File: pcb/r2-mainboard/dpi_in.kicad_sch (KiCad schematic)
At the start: 0 parts

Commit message: R2: WP7 -- dpi_in drawn, and a silent short caught before it reached fab
tools/gen_dpi_in.py draws dpi_in.kicad_sch: unit 2 of the PCM-071, 22 pins
fanning into the 22 hierarchical labels fpga_io has exported since WP5. No
components at all, which is also how the "nothing may load DPI_R6/DPI_R7" rule
is satisfied -- a sheet note says so, so a later reviewer does not add the
"missing" termination.

The bit mapping is the whole content of the sheet and the only thing that can
be wrong in a way that still boots: VOUT0_DATA<n> = DPI_PIXEL[n], channel =
BGR[n/6], bit = 2 + n%6, where the 2 is RGB666 keeping the top six bits of each
channel. Verified three ways -- the generator asserts the 22 net names are
exactly the expected set with no duplicates and that D2/D4 land on R6/R7; every
claimed pin is re-read from som_pinout.json; and the exported netlist is
cross-checked against Caster's own UCF, where all 18 DPI_PIXEL LOC constraints
land on the ball the schematic wires.

A REAL BUG, found by that netlist check and not by ERC. set_sheet_pins grew
dpi_in's root box from 25.4 mm to 63.5 mm to fit 22 pins, and the taller box
swallowed epd's. wire_root's stubs then landed inside epd's box and merged the
two sheets' nets: seven DPI_* nets came out shorted to the panel bus, so
DPI_R2 was the same net as EPDC_D0N, with J6.38 and a second U41 ball on it.
The schematic stayed perfectly legal and ERC said nothing.

This is the *second* time -- WP5 lost seven FPGA balls to VCOM_MEA_EN the same
way when fpga_io grew. The guard existed but lived in layout_root.py, which
nothing was obliged to call. Moved: layout_root.overlaps()/assert_no_overlap()
are now the shared implementation, and wire_root.py calls it before emitting
anything. wire_root is the right home because it is what turns sheet pins into
nets, so it is the last place the check can prevent the short rather than
report it afterwards. Confirmed the guard fires on the broken tree, then
layout_root re-packed the column and eve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
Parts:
- added X2: PCM-071, footprints:PCM-071_2xBTH-060-01-L-D-A-K, symbol r2:PCM-071
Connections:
- new net DPI_B2: X2.B12 (X_VOUT0_DATA0)
- new net DPI_B3: X2.B6 (X_VOUT0_DATA1)
- new net DPI_B4: X2.B4 (X_VOUT0_DATA2)
- new net DPI_B5: X2.B5 (X_VOUT0_DATA3)
- new net DPI_B6: X2.B7 (X_VOUT0_DATA4)
- new net DPI_B7: X2.B10 (X_VOUT0_DATA5)
- new net DPI_DE: X2.A15 (X_VOUT0_DE)
- new net DPI_G2: X2.B11 (X_VOUT0_DATA6)
- new net DPI_G3: X2.B9 (X_VOUT0_DATA7)
- new net DPI_G4: X2.B15 (X_VOUT0_DATA8)
- new net DPI_G5: X2.B14 (X_VOUT0_DATA9)
- new net DPI_G6: X2.A16 (X_VOUT0_DATA10)
- new net DPI_G7: X2.A11 (X_VOUT0_DATA11)
- new net DPI_HS: X2.A6 (X_VOUT0_HSYNC)
- new net DPI_PCLK: X2.A7 (X_VOUT0_PCLK)
- new net DPI_R2: X2.A8 (X_VOUT0_DATA12)
- new net DPI_R3: X2.A10 (X_VOUT0_DATA13)
- new net DPI_R4: X2.A12 (X_VOUT0_DATA14)
- new net DPI_R5: X2.A13 (X_VOUT0_DATA15)
- new net DPI_R6: X2.D2 (X_GPMC0_AD8/BOOTMODE_8)
- new net DPI_R7: X2.D4 (X_GPMC0_AD9/BOOTMODE_9)
- new net DPI_VS: X2.A5 (X_VOUT0_VSYNC)
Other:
- note added: "*** D2 and D4 are also BOOTMODE_8 and BOOTMODE_9, the primary boot mode"
- note added: "*** The absence of components here is deliberate. See docs/som.md 2."
- note added: "*** may load DPI_R6 or DPI_R7 -- no pull-up, pull-down or termination."
- note added: "*** selection, strapped high by 100K on the module. Nothing on this board"
- note added: "Bit mapping, from AM62x TRM Fig. 12-471 and Caster constraint.ucf:"
- note added: "RGB666 keeps the top six bits of each channel, so bit 2 is the LSB."
- note added: "VOUT0_DATA<n> = DPI_PIXEL[n]; channel = BGR[n/6], bit = 2 + n%6."
- note added: "X1 D2/D4 are named X_GPMC0_AD8/AD9 in the pinout tables. Table 31 is what"
- note added: "dpi_in -- the SoM's 18-bit RGB666 output into Caster. 22 signals, no parts."
- note added: "shows the module also drives them as VOUT0_DATA16/DATA17."

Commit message: R2: the six approved edits, and one of them was already done
Owner-approved 2026-08-19, KiCad closed for the pass.

1. R225 22k -> 20.5K/1%, LCSC C57105 (0402WGF2052TCE, UNI-ROYAL, the
   family the rest of the board already uses). Rendered and checked:
   R224 390k over R225 20.5k with R213 100k injecting VGH_DAC, so
   20.5||100 = 17.01k and VGH = 1.2 x (1 + 390/17.01) = 28.71 V at
   DAC = 0 -- exactly epd-port.md 10.3's target.
2. The five sense-divider caps that carried codes for the wrong
   capacitance -> C1523 (0402B102K500NT, 1 nF 50 V X7R, JLC Basic,
   5.3 M stock). One part covers both the 25 V and 50 V positions.
2b. R88/R224 -> C54920667 (HRC0402F3903DNTO, 390k 1%, 20 k stock).
   C25782 had 14 units against two per board. The owner found this one;
   both obvious alternatives were traps -- C23150 is 0603, and C44937
   is 3.9 ohm despite "390K" in its part number.
3. C147 set DNP rather than deleted. panel.md 7 had already ruled that
   J6.7/J6.44 stay; that covered the pins but not the capacitor on the
   dead net. DNP drops it from placement, keeps the topology of a frozen
   sheet untouched, and leaves the footprint if a future panel drives
   the rail. in_bom stays yes -- that is this board's convention for all
   13 DNP parts, so they show up flagged rather than vanishing.
4. Ten duplicate #PWR references renumbered to #PWR1112-1121 on the
   battery sheet, which was the colliding side in every case.
5. J3 was already deleted on 2026-08-15. No work needed.
6. Specter -> Reflow across 22 files: 14 sheets, 7 generators, the
   project file. .history/ deliberately untouched.

Verified as one change: netlist before and after has 518 nets with
identical pin membership, and epd_power and epd were rendered to PNG and
inspected.

Docs updated to match: epd-port.md 10 is applied rather than designed,
frontlight.md 1 loses the "9 in series is inferred" hedge (the vendor
listing confirms 2 x 9), and io-expansion.md 4's "only guess on this
sheet" is resolved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
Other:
- title: Glider-R2 / Specter mainboard -> Glider-R2 / Reflow mainboard
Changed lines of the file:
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@@
 	(paper "A3")
 	(title_block
-		(title "Glider-R2 / Specter mainboard")
+		(title "Glider-R2 / Reflow mainboard")
 		(date "2026-08-15")
 		(rev "A")

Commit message: R2: two interrupts that could never fire, and the SoM footprint
The EXTI collisions mcu.md §3.4 found are applied. An EXTI line is picked
by the pin's *number*, so TOUCH_INT# on PC3 was fighting PD3 GAUGE_ALRT#
and PEN_INT# on PC6 was fighting PD6 QON_SNS -- as drawn neither touch nor
pen could raise an interrupt at all. Each swaps with an output, which needs
no line, so it costs nothing. FL_INT# gets PB12 at the same time, which was
frontlight.md §10.3's own first suggestion; §9's later push for PB7 was
wrong, because PC7 KEY_PREV# holds EXTI7.

518 -> 517 nets, the drop being the PB12 unconnected- pseudo-net, and
exactly five membership changes. Every hierarchical label in the project
now has a counterpart -- DANGLING_OK is empty and ERC excluding
footprint_link_issues is 32, down from 105.

The PCM-071 footprint is built rather than downloaded, because two drawings
have landed that over-determine it: Samtec's own vector land pattern (parsed
from the content stream, every measurement agreeing with a printed dimension
to under 1 um) and L-1038e.A5 Figure 7, which is a carrier-board drawing.
The trap it contains is that the alignment hole is NOT on the connector's
centreline -- it is 1.054 mm from one row and 5.118 from the other, and
Figure 7 dimensions the holes, so assuming a centred hole puts both
connectors 2.06 mm out. The check worth trusting is the one nothing forces:
the B and C rows land 0.982 and 0.998 mm inside the module's edges.

Also: U41's speed grade is settled -2 -- LCSC has no -3 in FTG256 at all,
and caster.xise's -3 is ISE's untouched default (valueState="default"), not
a choice anyone made. But -2's MCB is rated 667 Mb/s against the 666.67 this
design runs, so fpga.md §1.1 asks for one free ISE build before the order.

And a bring-up landmine: epd_pos_rails_good() accepts VGH <= 28.0 V while
R2's own R225 change puts it at 28.41 V nominal. A correctly built board
would fatal() at every EPD power-up. epd-port.md §10.5.

Co-Authored-By: Claude Op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
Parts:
- X2: footprint footprints:PCM-071_2xBTH-060-01-L-D-A-K -> r2:PCM-071_2xBTH-060-01-L-D-A-K
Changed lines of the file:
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@@
 			)
 		)
-		(property "Footprint" "footprints:PCM-071_2xBTH-060-01-L-D-A-K"
+		(property "Footprint" "r2:PCM-071_2xBTH-060-01-L-D-A-K"
 			(at 127 130.81 0)
 			(hide yes)

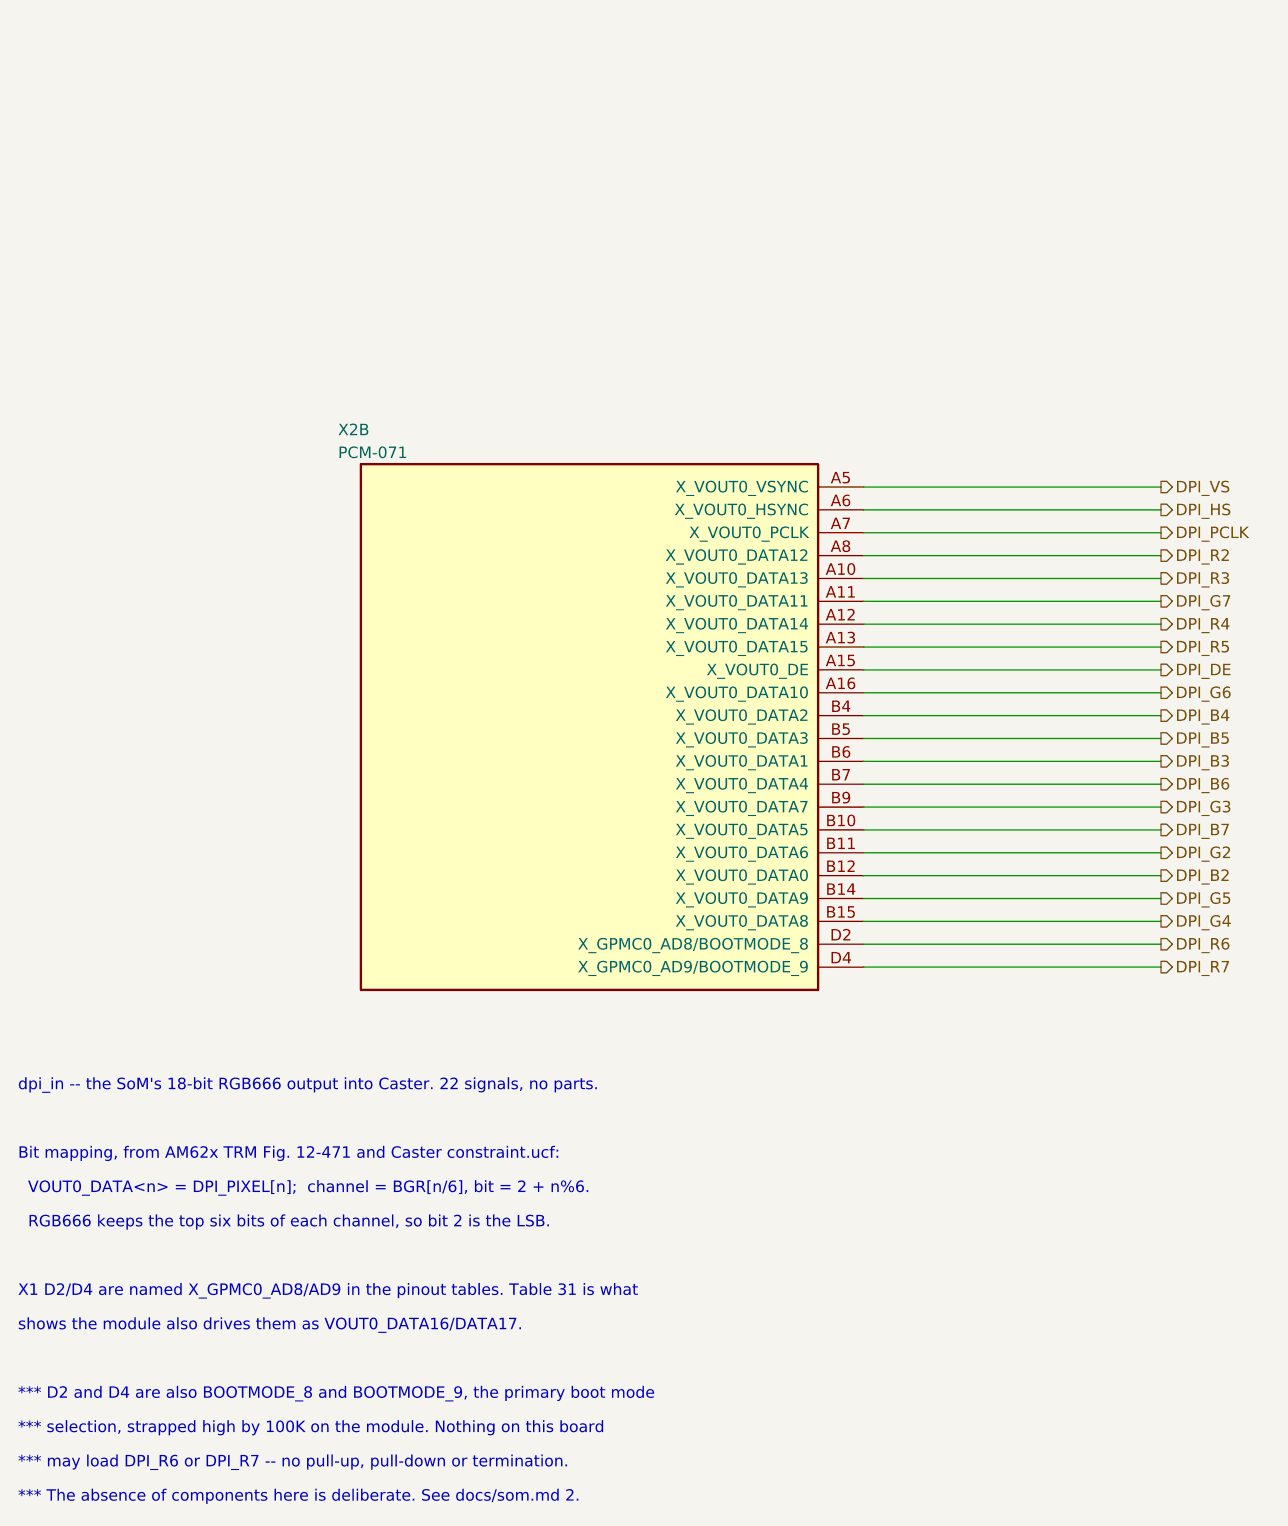
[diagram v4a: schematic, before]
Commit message: R2: the SoM is now two connectors, which is what the board has
The owner's call, and the right one: "I would rather have the two BTH
connectors and connect all signals/lines etc. to those two instead of the
A,B,... split. Then routing it later would also make more sense for me."
Clever loses to clear -- and the clever version could not be assembled
anyway, because a position file has one row per reference and there is no
single part covering 240 pads.

J26 carries the module's A and B columns, J27 its C and D, 120 pins each.
X2 survives as the module: outline and the two M2.5 holes, no pads, no
nets, excluded from the position file because it is fitted by hand. Three
footprints replace the one. Six unit boxes on som instead of three, two on
dpi_in instead of one; the root hierarchy is untouched.

What made this safe is that it is a repartition, not a renumber. Pin
numbers stay A1-A60 / B1-B60 / C1-C60 / D1-D60 exactly as L-1038e.A5
Tables 7-10 print them -- not Samtec's 1-120 alternating numbering -- and
the footprints name their pads the same way. Names, numbers and electrical
types are untouched; only which symbol a pin belongs to changes.

The acceptance test was exact: the netlist must be identical except every
X2.<pin> becomes J26.<pin> or J27.<pin> by row. It is -- 517 nets, 270
named nets with identical membership, 247 unconnected pins. ERC unchanged
at 32. Both sheets rendered and checked; two text collisions found that way
and fixed by deriving ref/val offsets from each box's own height.

check_pcb_connectors.py keeps the geometry guarantee the single footprint
used to give structurally, and now verifies it instead: J26 = X2 +
(-11.200, -2.400), J27 = X2 + (+11.200, +2.400), same side, same rotation,
122 pads each against the module's 2.

Two bugs fixed on the way, neither about the restructure. gen_som.py could
not find som_pinout.json -- it hardcoded datasheets/<name>, which broke in
the 2026-08-19 reorganisation; 058e9b9 fixed three tools and missed this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
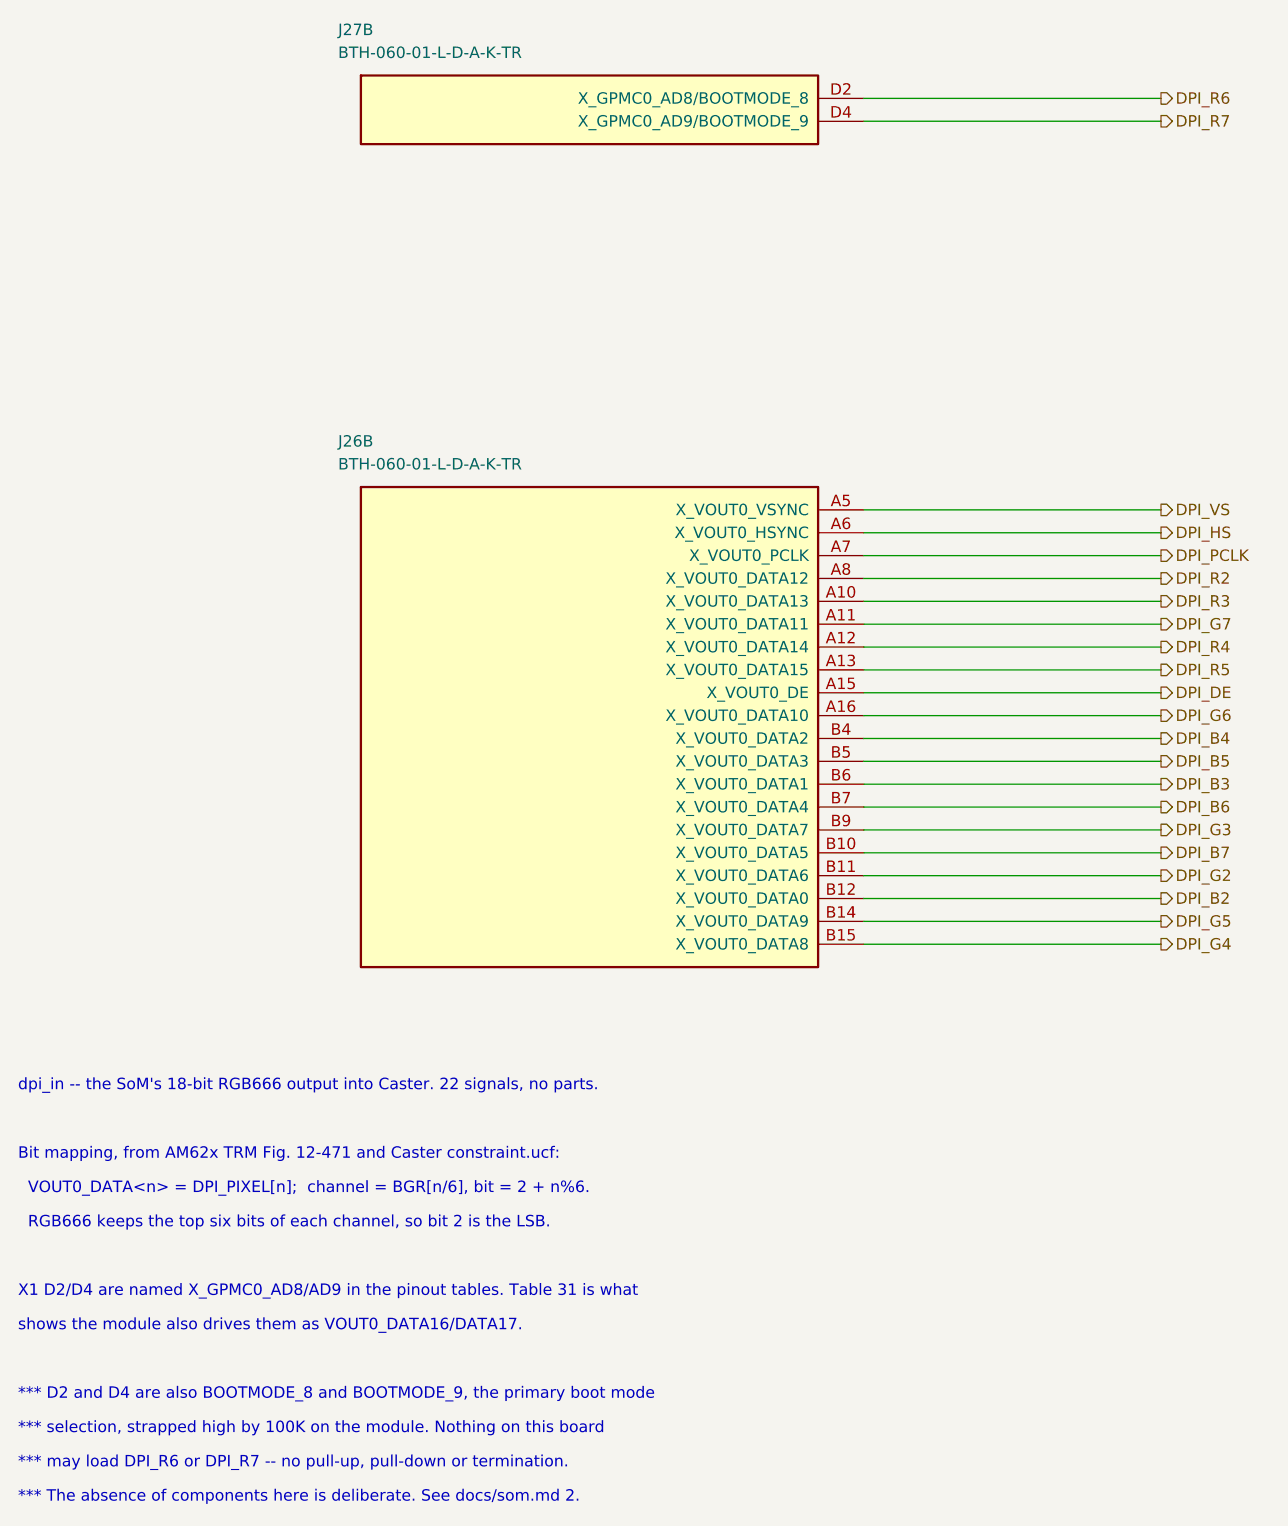
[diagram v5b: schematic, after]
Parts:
- removed X2: PCM-071, r2:PCM-071_2xBTH-060-01-L-D-A-K, symbol r2:PCM-071
- added J26: BTH-060-01-L-D-A-K-TR, r2:BTH-060-01-L-D-A-K_AB, symbol r2:BTH-060_AB
- added J27: BTH-060-01-L-D-A-K-TR, r2:BTH-060-01-L-D-A-K_CD, symbol r2:BTH-060_CD
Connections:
- net DPI_B2: now also J26.B12 (X_VOUT0_DATA0)
- net DPI_B3: now also J26.B6 (X_VOUT0_DATA1)
- net DPI_B4: now also J26.B4 (X_VOUT0_DATA2)
- net DPI_B5: now also J26.B5 (X_VOUT0_DATA3)
- net DPI_B6: now also J26.B7 (X_VOUT0_DATA4)
- net DPI_B7: now also J26.B10 (X_VOUT0_DATA5)
- net DPI_DE: now also J26.A15 (X_VOUT0_DE)
- net DPI_G2: now also J26.B11 (X_VOUT0_DATA6)
- net DPI_G3: now also J26.B9 (X_VOUT0_DATA7)
- net DPI_G4: now also J26.B15 (X_VOUT0_DATA8)
- net DPI_G5: now also J26.B14 (X_VOUT0_DATA9)
- net DPI_G6: now also J26.A16 (X_VOUT0_DATA10)
- net DPI_G7: now also J26.A11 (X_VOUT0_DATA11)
- net DPI_HS: now also J26.A6 (X_VOUT0_HSYNC)
- net DPI_PCLK: now also J26.A7 (X_VOUT0_PCLK)
- net DPI_R2: now also J26.A8 (X_VOUT0_DATA12)
- net DPI_R3: now also J26.A10 (X_VOUT0_DATA13)
- net DPI_R4: now also J26.A12 (X_VOUT0_DATA14)
- net DPI_R5: now also J26.A13 (X_VOUT0_DATA15)
- net DPI_R6: now also J27.D2 (X_GPMC0_AD8/BOOTMODE_8)
- net DPI_R7: now also J27.D4 (X_GPMC0_AD9/BOOTMODE_9)
- net DPI_VS: now also J26.A5 (X_VOUT0_VSYNC)

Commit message: R2: renumber every sheet to the page-based designator scheme
The owner's scheme is classifier + sheet page + two-digit part from 00. Four
sheets already used it; this converts the remaining nine, so all thirteen now
agree: pages 2-9 take three digits, pages 10-14 four. 292 of 333 designators
changed. A part shared by several sheets takes its lowest page, so the FPGA is
U700 (pages 7-9) and the two SoM connectors are J501/J502 (pages 5-6).

The whole risk here is silently rewiring the board, so the netlist was diffed
rather than eyeballed:

  nets 519 -> 519, total pin connections 1563 -> 1563
  named nets present in both whose pin multiset changed: 0
  ERC unchanged at 14 errors / 20 warnings
  check_ucf.py: 99 balls matched, 0 failures

That last one matters most: it resolves the gateware's 113 UCF constraints to
board nets *by ball name*, so it is the sharpest detector of the corruption
this change could cause.

Two earlier attempts did cause exactly that. A bare quoted-string substitution
also rewrites FPGA ball names (C1, D2, N11, T1) and BTH-060 pin names (A1-D60),
which are spelled exactly like designators; one run left ERC identical while 40
nets came back with a different pin multiset. The tool now substitutes only at
the two positions that store an instance's designator, and excludes every pin
name everywhere else. docs/layout.md 9.5 records the hazard and how to prove a
renumber was clean.

Only the three scripts that read the design are updated. The gen_*/patch_*/
port_r1.py scripts keep the old names deliberately: each wrote a sheet once and
has not been re-runnable since it was hand-edited in Eeschema, so they are a
historical record -- and port_r1.py's dict keys are R1 designators that were
never renumbered at all.

Co-Authored-By: Claude Opus 5 <noreply@anthropic.com>
Claude-Session: https://claude.ai/code/session_01MHTAe6ZnhogTEgtyPcLhwG
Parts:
- renumbered J26 to J501, J27 to J502
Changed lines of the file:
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@@
 		(in_pos_files yes)
 		(dnp no)
-		(property "Reference" "J27"
+		(property "Reference" "J502"
 			(at 99.06 53.34 0)
 			(show_name no)
@@
 			(project "r2"
 				(path "/dee825bf-c2f1-415d-afdf-cf702072a6e8/2428c127-2c5d-44de-b80a-89c491ec60c4"
-					(reference "J27")
+					(reference "J502")
 					(unit 2)
 				)
@@
 		(in_pos_files yes)
 		(dnp no)
-		(property "Reference" "J26"
+		(property "Reference" "J501"
 			(at 99.06 99.06 0)
 			(show_name no)
@@
 			(project "r2"
 				(path "/dee825bf-c2f1-415d-afdf-cf702072a6e8/2428c127-2c5d-44de-b80a-89c491ec60c4"
-					(reference "J26")
+					(reference "J501")
 					(unit 2)
 				)
